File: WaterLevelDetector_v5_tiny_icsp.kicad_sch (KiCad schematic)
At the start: 12 parts, among them J3 USB_C_Receptacle_PowerOnly_6P, J4 Conn_02x03_Odd_Even, U1 ATtiny85-20P

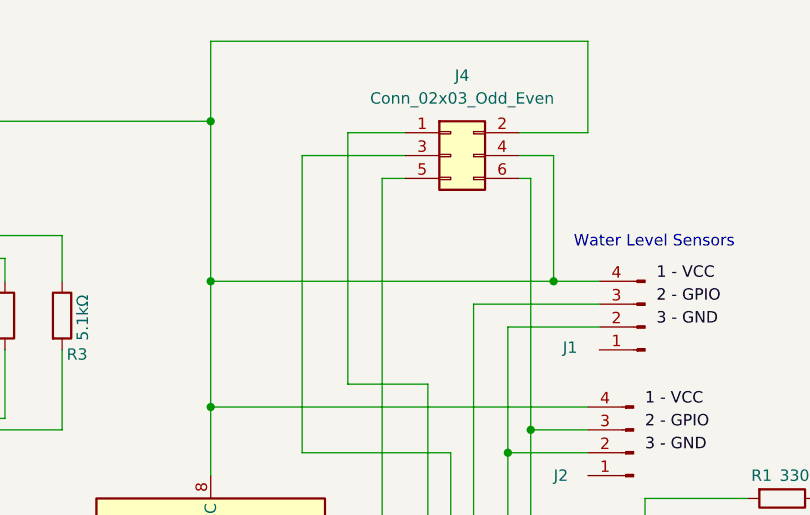
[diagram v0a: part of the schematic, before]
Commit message: made the pcb area smaller
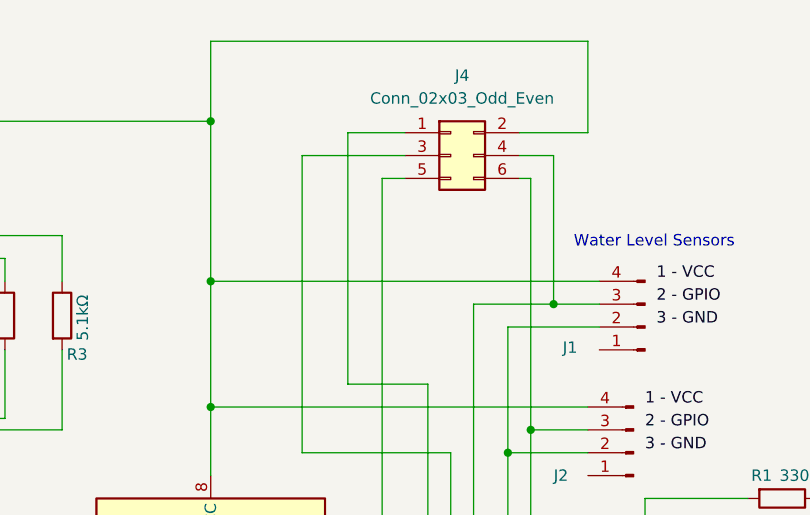
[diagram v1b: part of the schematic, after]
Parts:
- J4: footprint Connector_Molex:Molex_Mini-Fit_Jr_5566-06A_2x03_P4.20mm_Vertical -> Connector_PinHeader_2.54mm:PinHeader_2x03_P2.54mm_Vertical
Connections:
- net at J1.4 (Pin_4), J2.4 (Pin_4), J3.A9 (VBUS)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: no longer J4.4 (Pin_4)
- net at J1.3 (Pin_3), U1.5 (AREF/PB0): now also J4.4 (Pin_4)
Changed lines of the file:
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@@
+	)
+	(junction
+		(at 180.34 82.55)
+		(diameter 0)
+		(color 0 0 0 0)
 	)
 	(junction
@@
 	)
 	(junction
-		(at 180.34 80.01)
-		(diameter 0)
-		(color 0 0 0 0)
-	)
-	(junction
 		(at 226.06 111.76)
 		(diameter 0)
@@
 	(wire
 		(pts
-			(xy 180.34 66.04) (xy 180.34 80.01)
-		)
-		(stroke
-			(width 0)
-			(type default)
-		)
-	)
-	(wire
-		(pts
 			(xy 176.53 66.04) (xy 180.34 66.04)
 		)
@@
 	(wire
 		(pts
-			(xy 142.24 80.01) (xy 180.34 80.01)
+			(xy 142.24 80.01) (xy 185.42 80.01)
 		)
 		(stroke
@@
 	(wire
 		(pts
+			(xy 180.34 82.55) (xy 185.42 82.55)
+		)
+		(stroke
+			(width 0)
+			(type default)
+		)
+	)
+	(wire
+		(pts
 			(xy 152.4 99.06) (xy 168.91 99.06)
 		)
@@
 	(wire
 		(pts
-			(xy 171.45 82.55) (xy 185.42 82.55)
+			(xy 171.45 82.55) (xy 180.34 82.55)
 		)
 		(stroke
@@
 	(wire
 		(pts
+			(xy 180.34 66.04) (xy 180.34 82.55)
+		)
+		(stroke
+			(width 0)
+			(type default)
+		)
+	)
+	(wire
+		(pts
 			(xy 175.26 138.43) (xy 171.45 138.43)
 		)
@@
 		(pts
 			(xy 99.06 93.98) (xy 99.06 95.25)
-		)
-		(stroke
-			(width 0)
-			(type default)
-		)
-	)
-	(wire
-		(pts
-			(xy 180.34 80.01) (xy 185.42 80.01)
 		)
 		(stroke
@@
 			)
 		)
-		(property "Footprint" "Connector_Molex:Molex_Mini-Fit_Jr_5566-06A_2x03_P4.20mm_Vertical"
+		(property "Footprint" "Connector_PinHeader_2.54mm:PinHeader_2x03_P2.54mm_Vertical"
 			(at 168.91 66.04 0)
 			(effects

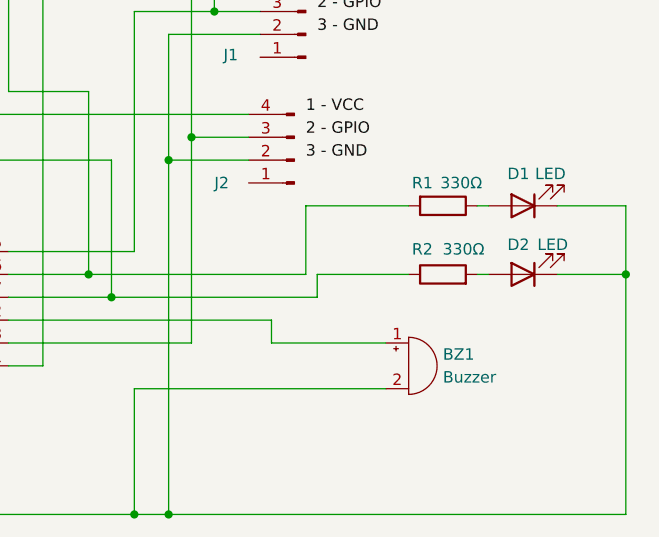
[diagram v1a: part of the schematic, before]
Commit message: hopefully made the leds red and green: schematic update
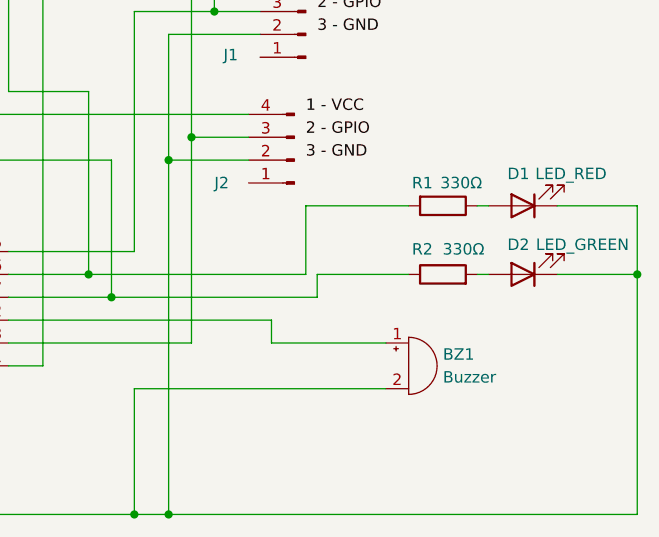
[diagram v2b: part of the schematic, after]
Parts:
- D1: value LED -> LED_RED
- D2: value LED -> LED_GREEN
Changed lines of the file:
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@@
+	)
+	(junction
+		(at 175.26 138.43)
+		(diameter 0)
+		(color 0 0 0 0)
 	)
 	(junction
@@
 	)
 	(junction
-		(at 226.06 111.76)
-		(diameter 0)
-		(color 0 0 0 0)
-	)
-	(junction
-		(at 175.26 138.43)
+		(at 227.33 111.76)
 		(diameter 0)
 		(color 0 0 0 0)
@@
 	(wire
 		(pts
+			(xy 218.44 111.76) (xy 227.33 111.76)
+		)
+		(stroke
+			(width 0)
+			(type default)
+		)
+	)
+	(wire
+		(pts
 			(xy 176.53 66.04) (xy 180.34 66.04)
 		)
@@
 	(wire
 		(pts
-			(xy 226.06 111.76) (xy 226.06 138.43)
+			(xy 227.33 111.76) (xy 227.33 138.43)
 		)
 		(stroke
@@
 	(wire
 		(pts
-			(xy 226.06 138.43) (xy 175.26 138.43)
-		)
-		(stroke
-			(width 0)
-			(type default)
-		)
-	)
-	(wire
-		(pts
 			(xy 99.06 96.52) (xy 99.06 138.43)
 		)
@@
 	(wire
 		(pts
+			(xy 218.44 104.14) (xy 227.33 104.14)
+		)
+		(stroke
+			(width 0)
+			(type default)
+		)
+	)
+	(wire
+		(pts
 			(xy 190.5 104.14) (xy 201.93 104.14)
 		)
@@
 	(wire
 		(pts
-			(xy 218.44 111.76) (xy 226.06 111.76)
+			(xy 175.26 138.43) (xy 227.33 138.43)
 		)
 		(stroke
@@
 	(wire
 		(pts
-			(xy 218.44 104.14) (xy 226.06 104.14)
-		)
-		(stroke
-			(width 0)
-			(type default)
-		)
-	)
-	(wire
-		(pts
 			(xy 185.42 85.09) (xy 175.26 85.09)
 		)
@@
 	(wire
 		(pts
-			(xy 226.06 104.14) (xy 226.06 111.76)
+			(xy 227.33 104.14) (xy 227.33 111.76)
 		)
 		(stroke
@@
 			)
 		)
-		(property "Value" "LED"
-			(at 217.678 100.584 0)
+		(property "Value" "LED_RED"
+			(at 219.964 100.584 0)
 			(effects
 				(font
@@
 			)
 		)
-		(property "Value" "LED"
-			(at 217.932 108.458 0)
+		(property "Value" "LED_GREEN"
+			(at 221.234 108.458 0)
 			(effects
 				(font
